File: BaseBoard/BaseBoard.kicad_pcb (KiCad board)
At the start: 4 copper layers, 50 x 35 mm, 46 parts, among them J1 locked, J2 Serial Port, J3 base connector, Q1 PMN48XP, SW2 boot, SW3 Reset, U1 ESP32-WROOM-E, U3 MCP73831-2ACI-OT, U4 XC6210B332MR

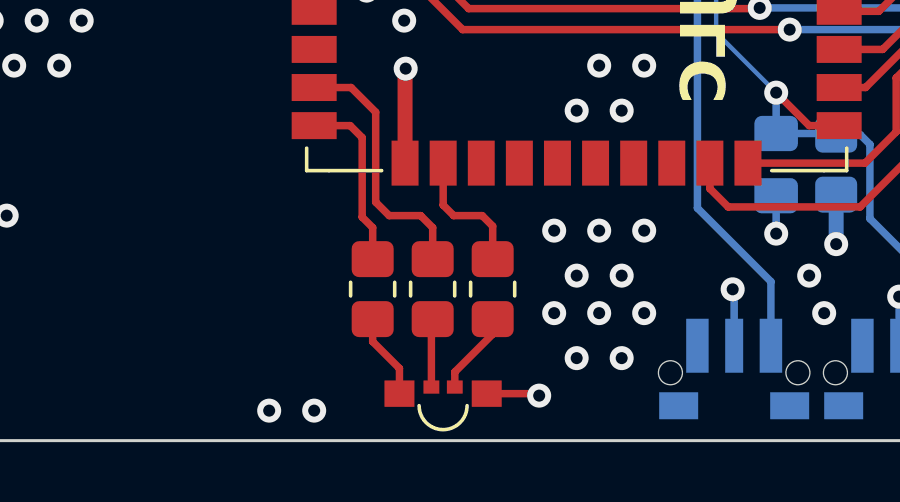
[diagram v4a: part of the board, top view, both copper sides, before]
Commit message: Reroutes pins for the LED
After fixing the schematic symbol, we needed to reflect the changes in
the layout.
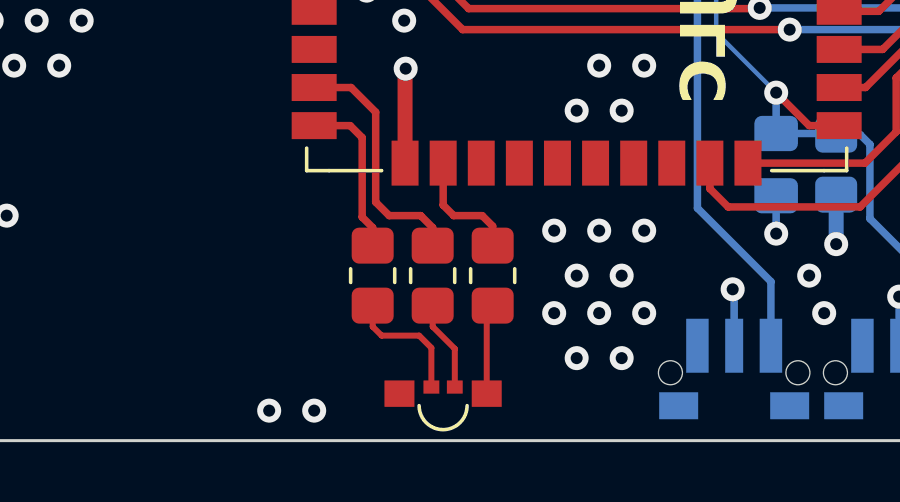
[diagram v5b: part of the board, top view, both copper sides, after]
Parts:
- moved R10 2.05 mm to (146.9, 109.5)
- moved R11 2.05 mm to (144.9, 109.5)
- moved R12 0.45 mm to (142.9, 109.5)
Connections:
- U1 pad 13: BAT_IND_R -> BAT_IND_G
- U1 pad 16: BAT_IND_G -> BAT_IND_R
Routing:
- net BAT_IND_R: track 8.69 -> 3.99 mm
- net BAT_IND_G: track 4.44 -> 8.24 mm
- net +3V3: track 36.3 -> 33.4 mm
- net Net-(D2-BK): track 2.28 -> 4.26 mm
- net Net-(D2-RK): track 1.77 -> 3.02 mm, vias 1 -> 0
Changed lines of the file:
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@@
       (net 36 "unconnected-(U1-ADC2_CH7/GPIO27)") (pinfunction "ADC2_CH7/GPIO27") (pintype "bidirectional+no_connect"))
     (pad "13" smd rect locked (at -8.75 8.23) (size 1.5 0.9) (layers "F.Cu" "F.Paste" "F.Mask")
-      (net 38 "BAT_IND_R") (pinfunction "MTMS/GPIO14/ADC2_CH6") (pintype "bidirectional"))
+      (net 39 "BAT_IND_G") (pinfunction "MTMS/GPIO14/ADC2_CH6") (pintype "bidirectional"))
     (pad "14" smd rect locked (at -8.75 9.5) (size 1.5 0.9) (layers "F.Cu" "F.Paste" "F.Mask")
       (net 40 "BAT_IND_B") (pinfunction "MTDI/GPIO12/ADC2_CH5") (pintype "bidirectional"))
@@
       (net 2 "GND") (pinfunction "GND") (pintype "power_in"))
     (pad "16" smd rect locked (at -4.45 10.75 90) (size 1.5 0.9) (layers "F.Cu" "F.Paste" "F.Mask")
-      (net 39 "BAT_IND_G") (pinfunction "MTCK/GPIO13/ADC2_CH4") (pintype "bidirectional"))
+      (net 38 "BAT_IND_R") (pinfunction "MTCK/GPIO13/ADC2_CH4") (pintype "bidirectional"))
     (pad "17" smd rect locked (at -3.18 10.75 90) (size 1.5 0.9) (layers "F.Cu" "F.Paste" "F.Mask")
       (net 41 "unconnected-(U1-NC)_1") (pinfunction "NC") (pintype "no_connect"))
@@
   )
   (footprint "Resistor_SMD:R_0805_2012Metric_Pad1.20x1.40mm_HandSolder" (layer "F.Cu")
-    (at 144.95 109.95 -90)
+    (at 146.95 109.5 -90)
     (descr "Resistor SMD 0805 (2012 Metric), square (rectangular) end terminal, IPC_7351 nominal with elongated pad for handsoldering. (Body size source: IPC-SM-782 page 72, https://www.pcb-3d.com/wordpress/wp-content/uploads/ipc-sm-782a_amendment_1_and_2.pdf), generated with kicad-footprint-generator")
     (tags "resistor handsolder")
@@
   )
   (footprint "Resistor_SMD:R_0805_2012Metric_Pad1.20x1.40mm_HandSolder" (layer "F.Cu")
-    (at 142.95 109.95 -90)
+    (at 142.95 109.5 -90)
     (descr "Resistor SMD 0805 (2012 Metric), square (rectangular) end terminal, IPC_7351 nominal with elongated pad for handsoldering. (Body size source: IPC-SM-782 page 72, https://www.pcb-3d.com/wordpress/wp-content/uploads/ipc-sm-782a_amendment_1_and_2.pdf), generated with kicad-footprint-generator")
     (tags "resistor handsolder")
@@
   )
   (footprint "Resistor_SMD:R_0805_2012Metric_Pad1.20x1.40mm_HandSolder" (layer "F.Cu")
-    (at 146.95 109.95 -90)
+    (at 144.95 109.5 -90)
     (descr "Resistor SMD 0805 (2012 Metric), square (rectangular) end terminal, IPC_7351 nominal with elongated pad for handsoldering. (Body size source: IPC-SM-782 page 72, https://www.pcb-3d.com/wordpress/wp-content/uploads/ipc-sm-782a_amendment_1_and_2.pdf), generated with kicad-footprint-generator")
     (tags "resistor handsolder")
@@
   (segment (start 165.022095 97.922095) (end 164.51574 97.922095) (width 0.25) (layer "F.Cu") (net 3))
   (segment (start 164.167262 105.96) (end 163.15 105.96) (width 0.25) (layer "F.Cu") (net 3))
-  (segment (start 142.95 111.7) (end 143.8425 112.5925) (width 0.25) (layer "F.Cu") (net 3))
   (segment (start 136.7 89.5375) (end 137 89.2375) (width 0.5) (layer "F.Cu") (net 3))
-  (segment (start 142.95 110.95) (end 142.95 111.7) (width 0.25) (layer "F.Cu") (net 3))
   (segment (start 165.002299 100.997701) (end 165.8 100.2) (width 0.25) (layer "F.Cu") (net 3))
   (segment (start 165.8 98.7) (end 165.022095 97.922095) (width 0.25) (layer "F.Cu") (net 3))
-  (segment (start 143.8425 112.5925) (end 143.8425 113.434368) (width 0.25) (layer "F.Cu") (net 3))
   (segment (start 164.512299 100.997701) (end 165.002299 100.997701) (width 0.25) (layer "F.Cu") (net 3))
   (segment (start 165.763848 86.77) (end 165.298848 86.77) (width 0.15) (layer "F.Cu") (net 3))
@@
   (segment (start 127.625 94.55) (end 127.875 94.3) (width 0.5) (layer "F.Cu") (net 10))
   (segment (start 132.275 95.55) (end 132.375 95.45) (width 0.5) (layer "F.Cu") (net 10))
-  (segment (start 148.434368 113.434368) (end 148.5 113.5) (width 0.25) (layer "F.Cu") (net 11))
-  (segment (start 146.7525 113.434368) (end 148.434368 113.434368) (width 0.25) (layer "F.Cu") (net 11))
-  (via (at 148.5 113.5) (size 0.8) (drill 0.4) (layers "F.Cu" "B.Cu") (net 11))
-  (segment (start 145.6875 113.214368) (end 145.6875 112.7125) (width 0.25) (layer "F.Cu") (net 12))
-  (segment (start 146.95 111.45) (end 146.95 110.95) (width 0.25) (layer "F.Cu") (net 12))
-  (segment (start 145.6875 112.7125) (end 146.95 111.45) (width 0.25) (layer "F.Cu") (net 12))
-  (segment (start 144.9075 113.214368) (end 144.9075 110.9925) (width 0.25) (layer "F.Cu") (net 13))
-  (segment (start 144.9075 110.9925) (end 144.95 110.95) (width 0.25) (layer "F.Cu") (net 13))
+  (segment (start 146.7525 113.434368) (end 146.7525 110.6975) (width 0.2) (layer "F.Cu") (net 11))
+  (segment (start 146.7525 110.6975) (end 146.95 110.5) (width 0.2) (layer "F.Cu") (net 11))
+  (segment (start 144.95 111.2) (end 145.6875 111.9375) (width 0.2) (layer "F.Cu") (net 12))
+  (segment (start 145.6875 111.9375) (end 145.6875 113.214368) (width 0.2) (layer "F.Cu") (net 12))
+  (segment (start 144.95 110.5) (end 144.95 111.2) (width 0.2) (layer "F.Cu") (net 12))
+  (segment (start 144.9075 113.214368) (end 144.9075 111.9075) (width 0.2) (layer "F.Cu") (net 13))
+  (segment (start 143.25 111.5) (end 142.95 111.2) (width 0.2) (layer "F.Cu") (net 13))
+  (segment (start 142.95 111.2) (end 142.95 110.5) (width 0.2) (layer "F.Cu") (net 13))
+  (segment (start 144.5 111.5) (end 143.25 111.5) (width 0.2) (layer "F.Cu") (net 13))
+  (segment (start 144.9075 111.9075) (end 144.5 111.5) (width 0.2) (layer "F.Cu") (net 13))
   (segment (start 124.5125 93.5) (end 126.45 93.5) (width 0.25) (layer "F.Cu") (net 14))
   (segment (start 141 93.07) (end 142.37 93.07) (width 0.25) (layer "F.Cu") (net 14))
@@
   (segment (start 121.35 89.8) (end 122.25 89.8) (width 0.25) (layer "F.Cu") (net 37))
   (segment (start 120.85 90.3) (end 121.35 89.8) (width 0.25) (layer "F.Cu") (net 37))
-  (segment (start 144.55 107.5) (end 144.95 107.9) (width 0.25) (layer "F.Cu") (net 38))
-  (segment (start 143.5 107.5) (end 144.55 107.5) (width 0.25) (layer "F.Cu") (net 38))
-  (segment (start 144.95 107.9) (end 144.95 108.95) (width 0.25) (layer "F.Cu") (net 38))
-  (segment (start 141 103.23) (end 142.23 103.23) (width 0.25) (layer "F.Cu") (net 38))
-  (segment (start 143.05 104.05) (end 143.05 107.05) (width 0.25) (layer "F.Cu") (net 38))
-  (segment (start 143.05 107.05) (end 143.5 107.5) (width 0.25) (layer "F.Cu") (net 38))
-  (segment (start 142.23 103.23) (end 143.05 104.05) (width 0.25) (layer "F.Cu") (net 38))
-  (segment (start 145.3 105.75) (end 145.3 107.15) (width 0.25) (layer "F.Cu") (net 39))
-  (segment (start 145.65 107.5) (end 146.6 107.5) (width 0.25) (layer "F.Cu") (net 39))
-  (segment (start 146.95 107.85) (end 146.95 108.95) (width 0.25) (layer "F.Cu") (net 39))
-  (segment (start 145.3 107.15) (end 145.65 107.5) (width 0.25) (layer "F.Cu") (net 39))
-  (segment (start 146.6 107.5) (end 146.95 107.85) (width 0.25) (layer "F.Cu") (net 39))
-  (segment (start 142.95 107.9) (end 142.95 108.95) (width 0.25) (layer "F.Cu") (net 40))
-  (segment (start 141 104.5) (end 142.2 104.5) (width 0.25) (layer "F.Cu") (net 40))
+  (segment (start 146.95 107.85) (end 146.95 108.5) (width 0.25) (layer "F.Cu") (net 38))
+  (segment (start 145.3 107.15) (end 145.65 107.5) (width 0.25) (layer "F.Cu") (net 38))
+  (segment (start 146.6 107.5) (end 146.95 107.85) (width 0.25) (layer "F.Cu") (net 38))
+  (segment (start 145.3 105.75) (end 145.3 107.15) (width 0.25) (layer "F.Cu") (net 38))
+  (segment (start 145.65 107.5) (end 146.6 107.5) (width 0.25) (layer "F.Cu") (net 38))
+  (segment (start 143.05 104.05) (end 143.05 107.05) (width 0.25) (layer "F.Cu") (net 39))
+  (segment (start 144.55 107.5) (end 144.95 107.9) (width 0.25) (layer "F.Cu") (net 39))
+  (segment (start 143.05 107.05) (end 143.5 107.5) (width 0.25) (layer "F.Cu") (net 39))
+  (segment (start 144.95 107.9) (end 144.95 108.5) (width 0.25) (layer "F.Cu") (net 39))
+  (segment (start 141 103.23) (end 142.23 103.23) (width 0.25) (layer "F.Cu") (net 39))
+  (segment (start 142.23 103.23) (end 143.05 104.05) (width 0.25) (layer "F.Cu") (net 39))
+  (segment (start 143.5 107.5) (end 144.55 107.5) (width 0.25) (layer "F.Cu") (net 39))
   (segment (start 142.2 104.5) (end 142.6 104.9) (width 0.25) (layer "F.Cu") (net 40))
   (segment (start 142.6 104.9) (end 142.6 107.55) (width 0.25) (layer "F.Cu") (net 40))
+  (segment (start 141 104.5) (end 142.2 104.5) (width 0.25) (layer "F.Cu") (net 40))
   (segment (start 142.6 107.55) (end 142.95 107.9) (width 0.25) (layer "F.Cu") (net 40))
+  (segment (start 142.95 107.9) (end 142.95 108.5) (width 0.25) (layer "F.Cu") (net 40))
   (zone (net 0) (net_name "") (layers "F.Cu" "In1.Cu" "In2.Cu" "B.Cu") (name "Antenna_keepout") (hatch edge 0.508)
     (connect_pads (clearance 0))

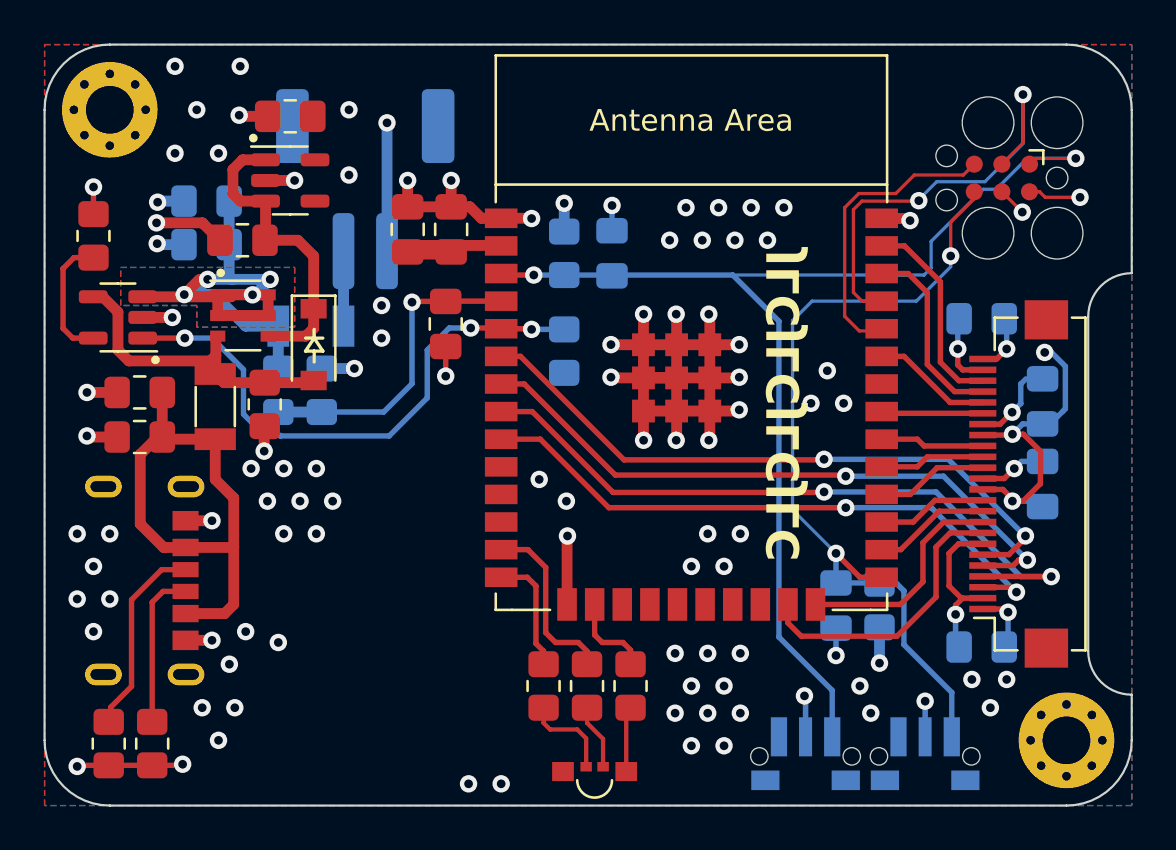
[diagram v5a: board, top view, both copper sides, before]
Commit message: Adds unused pins to the add-on connector
Those pins were used to get the ID from the DIP switches, but since we
don't have them anymore, we can use them as GPIOs.

This commit changes the connector on the baseboard (including rerouting
the traces) and updates the add-on connector schematic symbol in the
symbol library, but does not update yet the boards that use the add-on
connector (sensor board and breakout board).
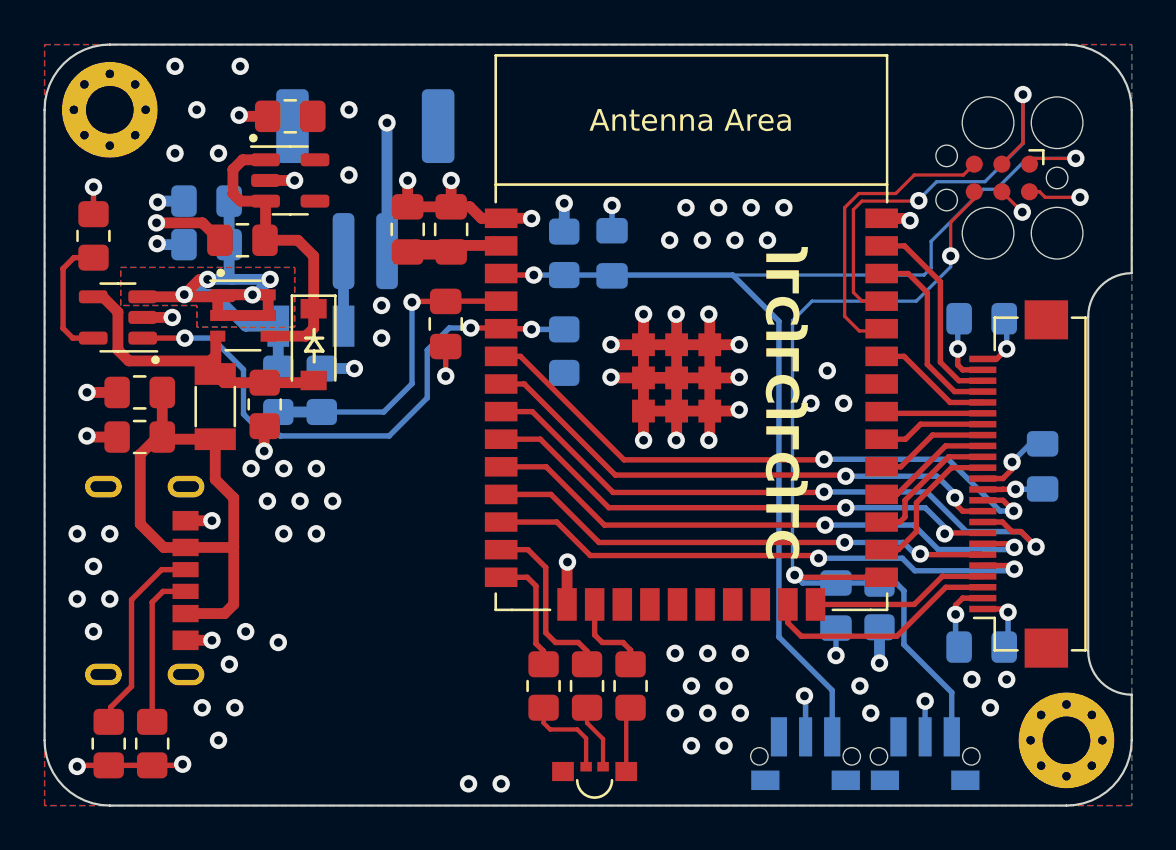
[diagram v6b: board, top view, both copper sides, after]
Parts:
- removed C8: 100nF, Capacitor_SMD:C_0805_2012Metric_Pad1.18x1.45mm_HandSolder
- moved C10 0.81 mm to (165.9, 99.4)
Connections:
- J3 pad 10: IO4 -> IO35
- J3 pad 11: IO16 -> IO34
- J3 pad 14: IO17 -> IO4
- J3 pad 15: IO5 -> IO16
- J3 pad 16: IO18 -> IO17
- J3 pad 17: +3V3 -> IO5
- J3 pad 18: GND -> IO18
- J3 pad 3: IO33 -> IO15
- J3 pad 4: IO32 -> IO2
- J3 pad 5: IO35 -> IO27
- J3 pad 6: IO34 -> IO26
- J3 pad 7: GND -> IO25
- J3 pad 8: IO15 -> IO33
- J3 pad 9: IO2 -> IO32
- U1 pad 10: unconnected-(U1-DAC_1/ADC2_CH8/GPIO25) -> IO25
- U1 pad 11: unconnected-(U1-DAC_2/ADC2_CH9/GPIO26) -> IO26
- U1 pad 12: unconnected-(U1-ADC2_CH7/GPIO27) -> IO27
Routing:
- net IO25: track 0.00 -> 26.7 mm, vias 0 -> 2
- net IO27: track 0.00 -> 26.1 mm, vias 0 -> 2
- net IO26: track 0.00 -> 23.3 mm, vias 0 -> 2
- net +3V3: track 33.4 -> 20.9 mm, vias 71 -> 63
- net GND: track 102.7 -> 94.5 mm, vias 42 -> 41
- net IO35: track 29.7 -> 24.8 mm
- net IO33: track 28.3 -> 24.1 mm
- net ESP_BOOT: track 38.5 -> 40.9 mm
- net IO15: track 13.4 -> 11.0 mm
- net IO2: track 10.3 -> 8.22 mm
- net IO34: track 29.9 -> 28.2 mm
- net IO4: track 5.38 -> 6.99 mm
- net IO32: track 31.6 -> 30.1 mm
- net IO16: track 5.06 -> 6.34 mm

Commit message: Creates separate footprint for add-on and base connector
They now have marks where they need to connect together which makes it
easier on the user since they are flipped relative to each other.

I also add the 3D model for another connector. It's not correct, but I
changed my mind again about having them.
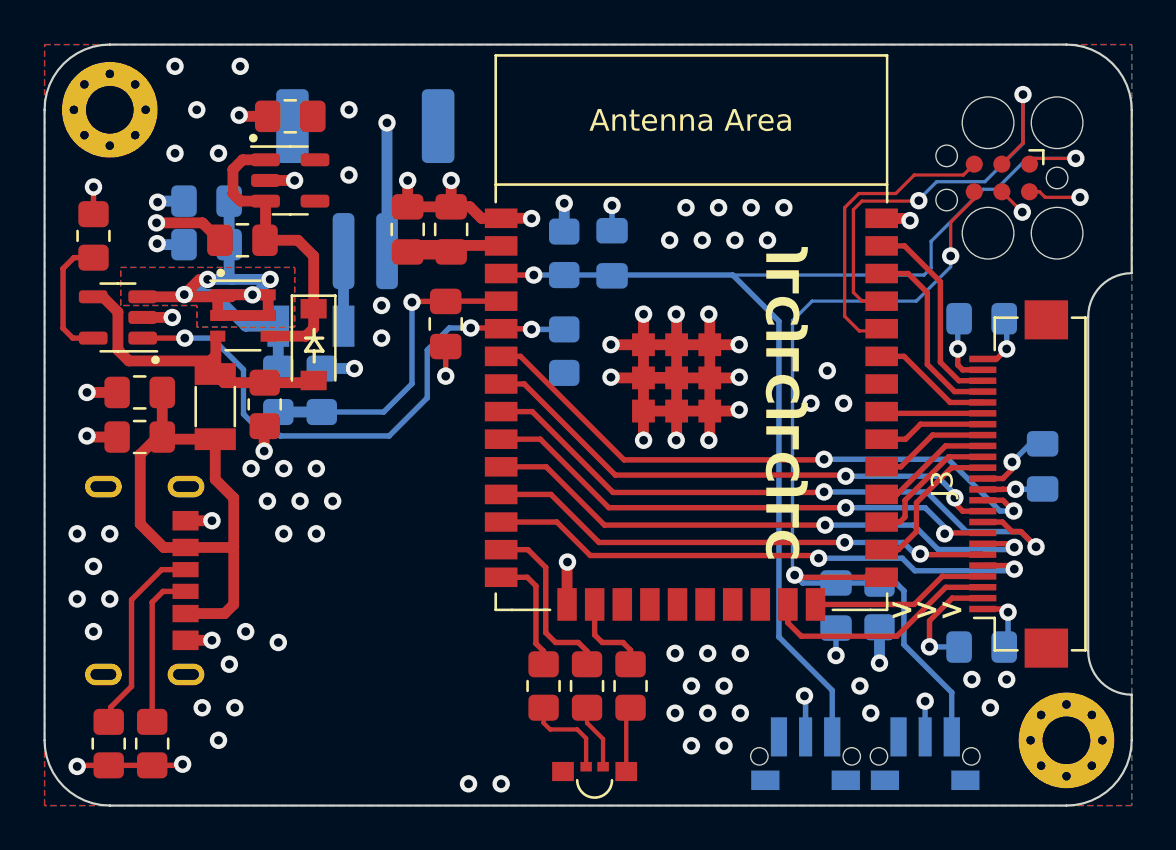
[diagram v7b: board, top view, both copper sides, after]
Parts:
- J3: footprint GameOver:TXGA_FFC05036-24SBD113W5M_1x24_P0.50mm_Horizontal -> GameOver:Base_conn_TXGA_FFC05036-24SBD113W5M_1x24_P0.50mm_Horizontal
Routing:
- net GND: track 94.5 -> 96.6 mm
